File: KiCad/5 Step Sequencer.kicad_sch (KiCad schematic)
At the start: 64 parts, among them J1 RESET IN, J2 TRIG IN, J4 CV OUT, J5 TRIG OUT, Q1 2SA1015, SW1 SW_DPST_x2, SW2 SW_DPST_x2, SW3 SW_DPST_x2, SW4 SW_DPST_x2, SW5 SW_DPST_x2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

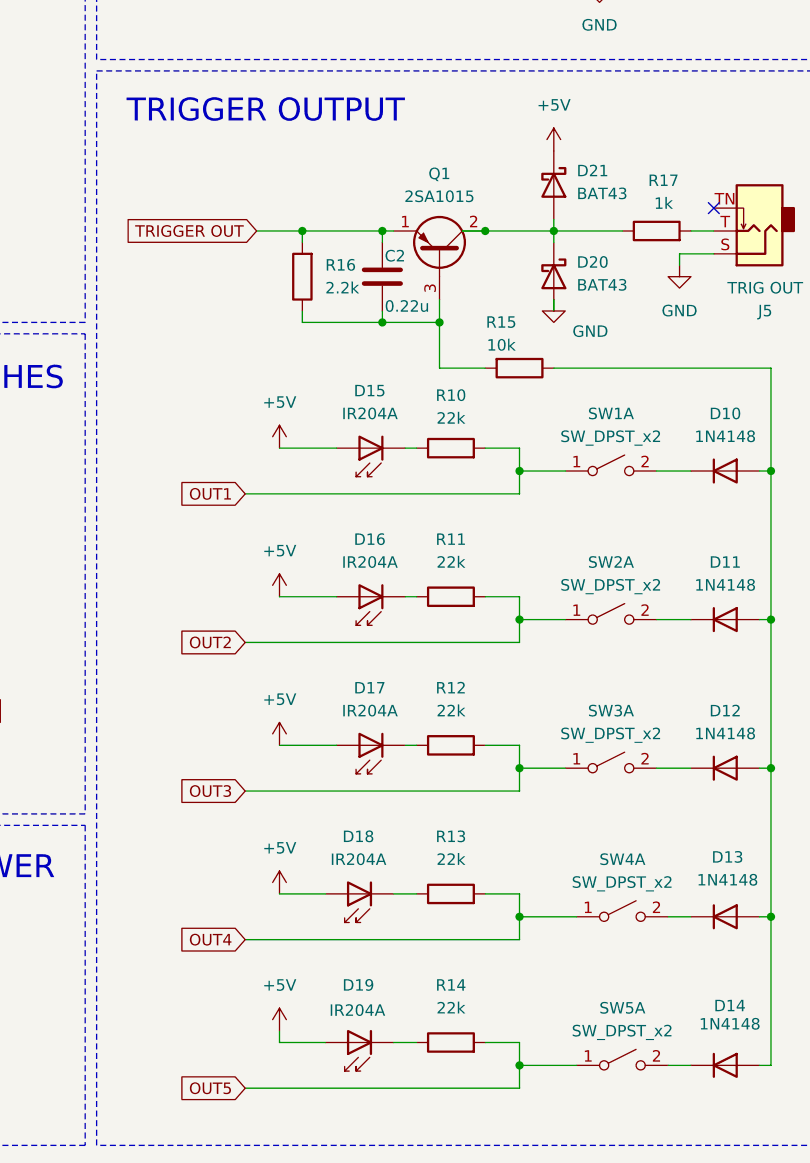
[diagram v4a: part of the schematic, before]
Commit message: adding some missing footprints
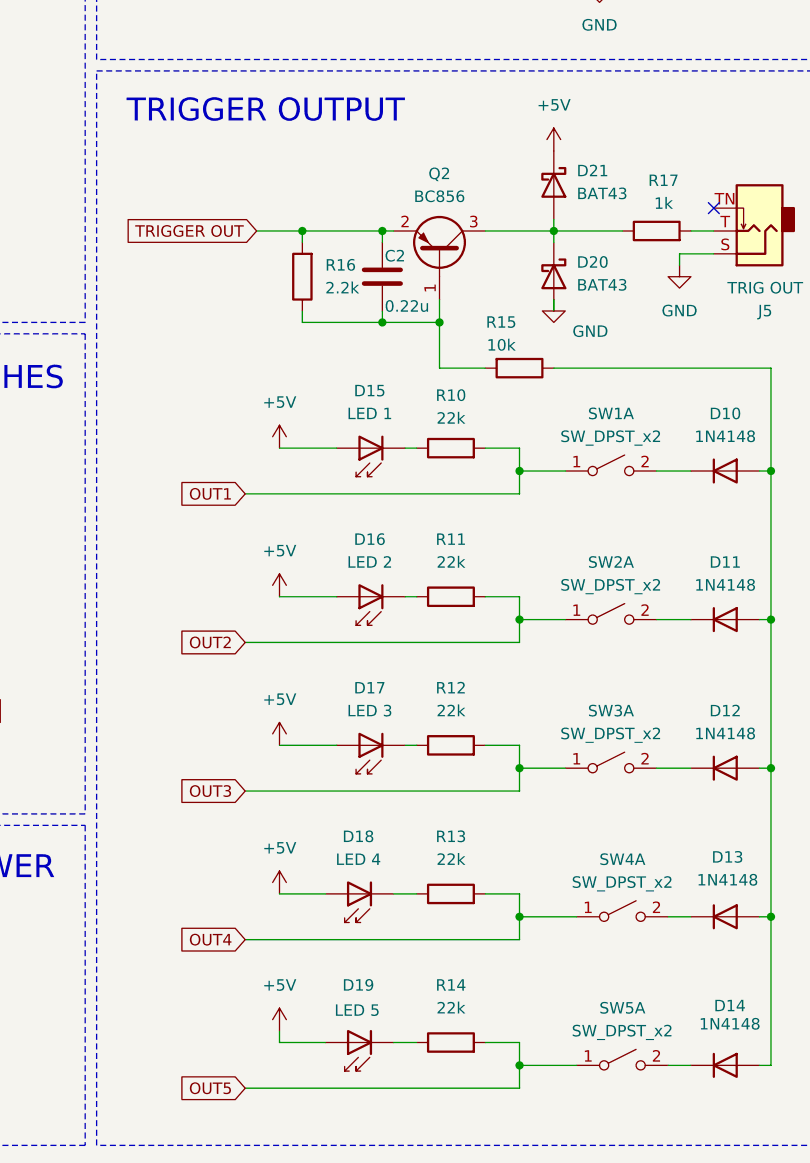
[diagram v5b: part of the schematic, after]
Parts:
- removed Q1: 2SA1015, Package_TO_SOT_THT:TO-92_Inline, symbol Transistor_BJT:2SA1015
- added Q2: BC856, Package_TO_SOT_SMD:SOT-23, symbol Transistor_BJT:BC856
- A1: footprint Module:Arduino_Nano -> Eurorack:Arduino_Nano; now left out of the parts list
- C1, C2, C3: footprint (none) -> Capacitor_SMD:C_0805_2012Metric_Pad1.18x1.45mm_HandSolder; now left out of the parts list
- C12, C13: now left out of the parts list
- D1, D10, D11, D12, D13, D14, D2, D20, D21, D3, D4, D5, D6, D7, D8, D9: footprint Diode_THT:D_DO-35_SOD27_P7.62mm_Horizontal -> Diode_SMD:D_SOD-323_HandSoldering; now left out of the parts list
- D15: value IR204A -> LED 1; footprint LED_THT:LED_D3.0mm_IRBlack -> LED_THT:LED_D3.0mm_Clear; now left out of the parts list
- D16: value IR204A -> LED 2; footprint LED_THT:LED_D3.0mm_IRBlack -> LED_THT:LED_D3.0mm_Clear; now left out of the parts list
- D17: value IR204A -> LED 3; footprint LED_THT:LED_D3.0mm_IRBlack -> LED_THT:LED_D3.0mm_Clear; now left out of the parts list
- D18: value IR204A -> LED 4; footprint LED_THT:LED_D3.0mm_IRBlack -> LED_THT:LED_D3.0mm_Clear; now left out of the parts list
- D19: value IR204A -> LED 5; footprint LED_THT:LED_D3.0mm_IRBlack -> LED_THT:LED_D3.0mm_Clear; now left out of the parts list
- J1, J2, J4, J5: footprint (none) -> Eurorack:Jack_3.5mm_QingPu_WQP-PJ398SM_Vertical; now left out of the parts list
- R1, R10, R11, R12, R13, R14, R15, R16, R17, R18, R2, R3, R4, R5, R6, R7, R8, R9: footprint (none) -> Resistor_SMD:R_0805_2012Metric_Pad1.20x1.40mm_HandSolder; now left out of the parts list
- RV1, RV2, RV3, RV4, RV5, RV6, RV7: footprint (none) -> Eurorack:Potentiometer_Alpha_RD901F_Vertical_Alt; now left out of the parts list
- SW1, SW2, SW3, SW4, SW5: footprint (none) -> Eurorack:Switch_Toggle_Dailywell_MS1T1B1M2QES_SPDT; now left out of the parts list
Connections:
- net TRIGGER OUT: now also Q2.2 (E)
- net at C2.2, R15.2, R16.1: now also Q2.1 (B)
- net at D20.1 (K), D21.2 (A), R17.1: now also Q2.3 (C)

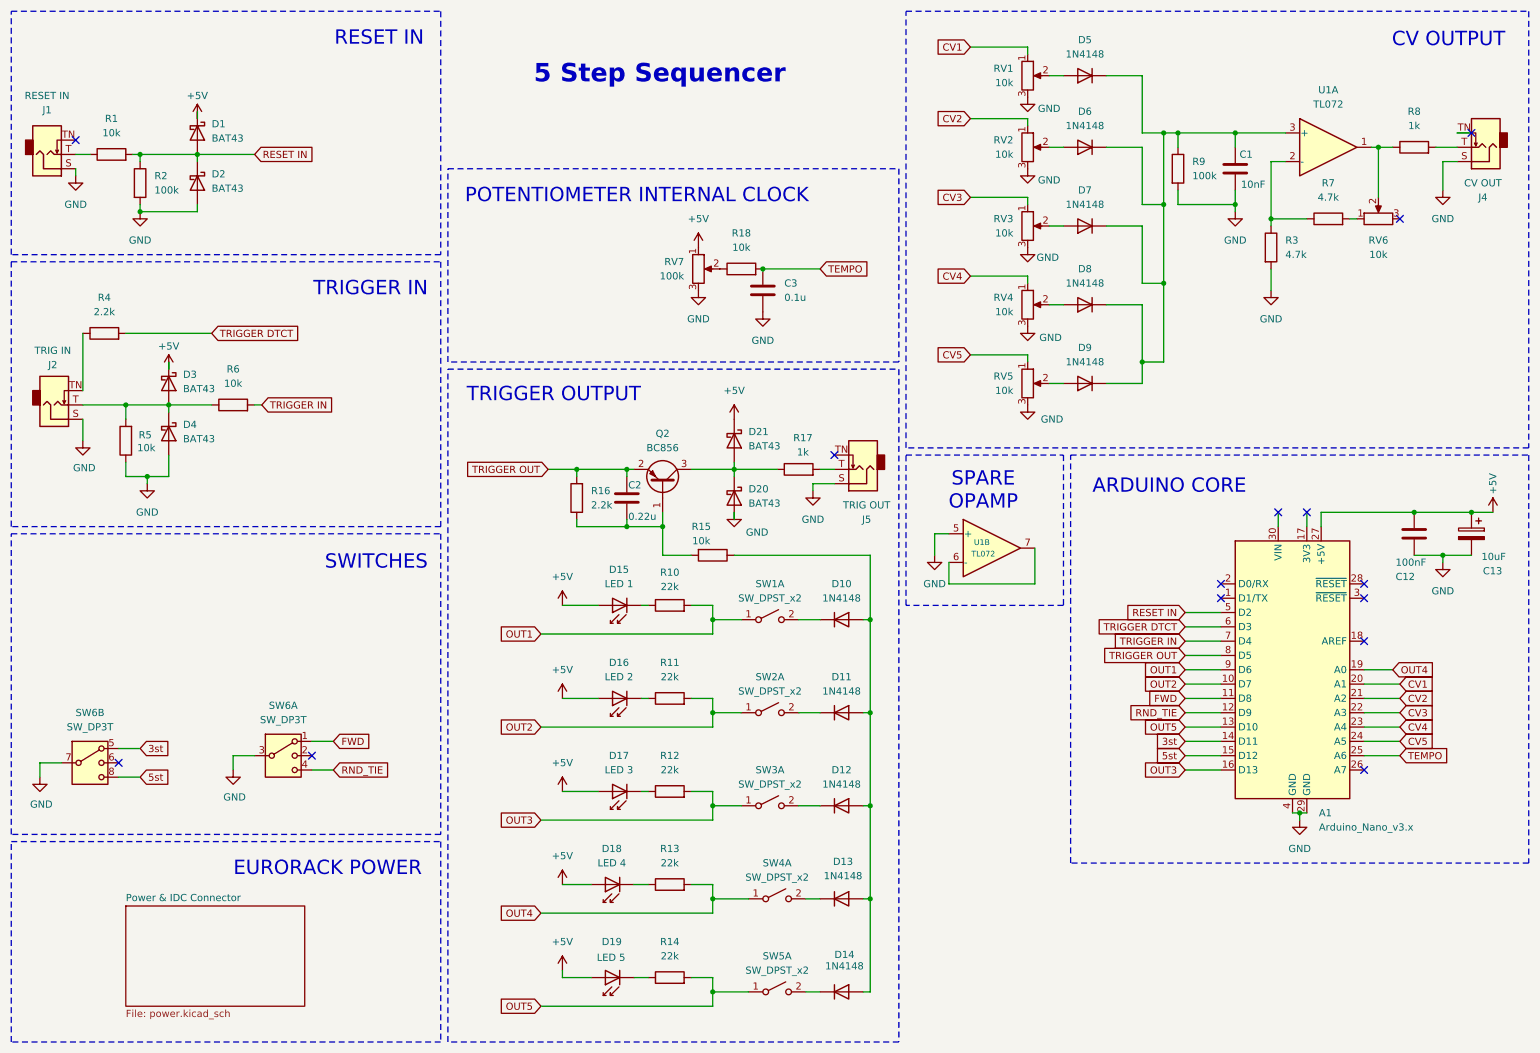
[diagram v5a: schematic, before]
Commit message: Changing Toggle Switch Foorptint
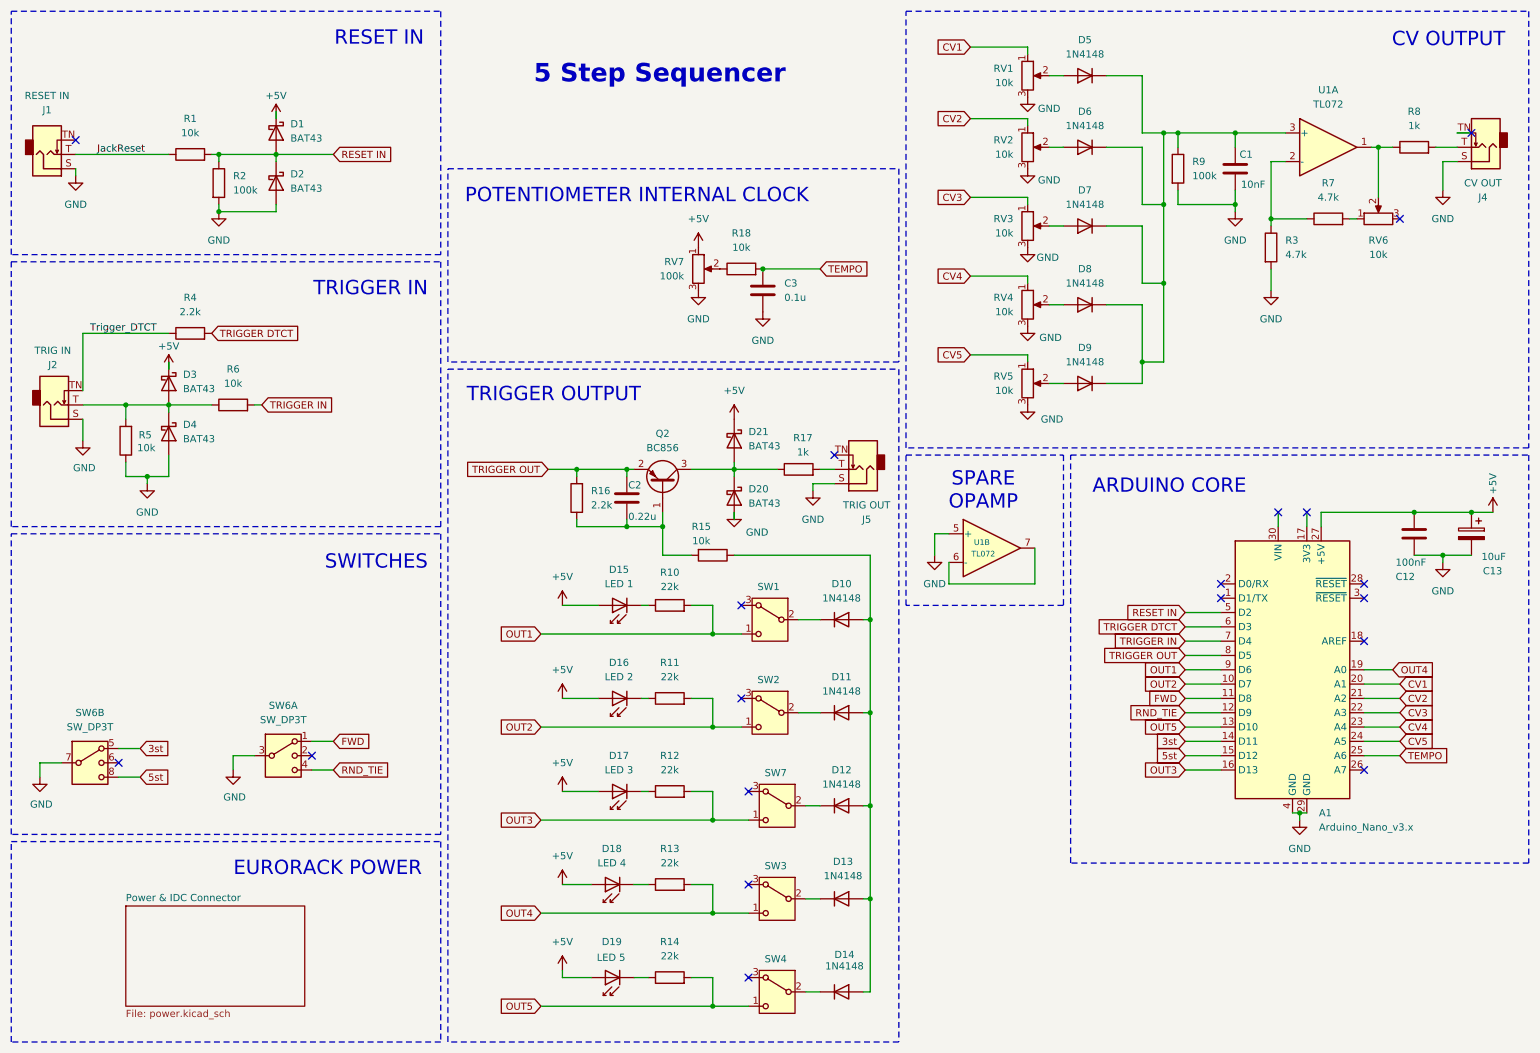
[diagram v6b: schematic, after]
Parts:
- removed SW1, SW2, SW3, SW4, SW5: SW_DPST_x2, Eurorack:Switch_Toggle_Dailywell_MS1T1B1M2QES_SPDT, symbol Switch:SW_DPST_x2
- added SW1, SW2, SW3, SW4, SW7: SW_SPDT_321, Eurorack:Switch_Toggle_Dailywell_MS1T1B1M2QES_SPDT, symbol Switch:SW_SPDT_321
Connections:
- net OUT1: now also SW1.1 (C)
- net OUT2: now also SW2.1 (C)
- net OUT3: now also SW7.1 (C)
- net OUT4: now also SW3.1 (C)
- net OUT5: now also SW4.1 (C)
- net Trigger_DTCT: now reaches J2.TN, R4.1
- net at D11.1 (K): now also SW2.2 (B)
- net at D10.1 (K): now also SW1.2 (B)
- net JackReset: now reaches J1.T, R1.1
- net at D13.1 (K): now also SW3.2 (B)
- net at D12.1 (K): now also SW7.2 (B)
- net at D14.1 (K): now also SW4.2 (B)
- no-connect marks 14 -> 19
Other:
- moved on the sheet: D1, D2, R1, R2, R4

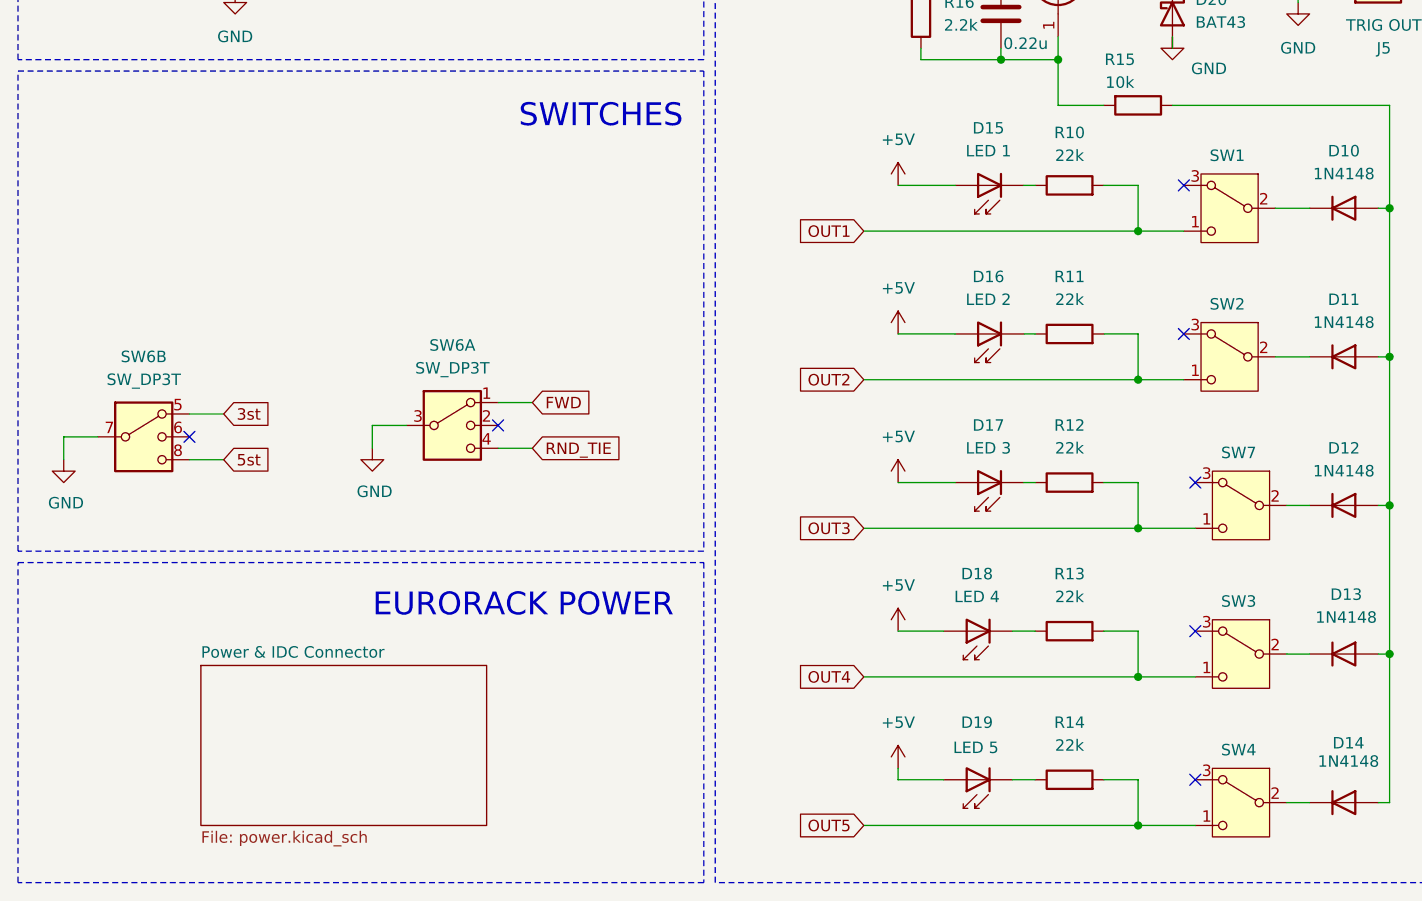
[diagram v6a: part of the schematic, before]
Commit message: adding last missing footprints
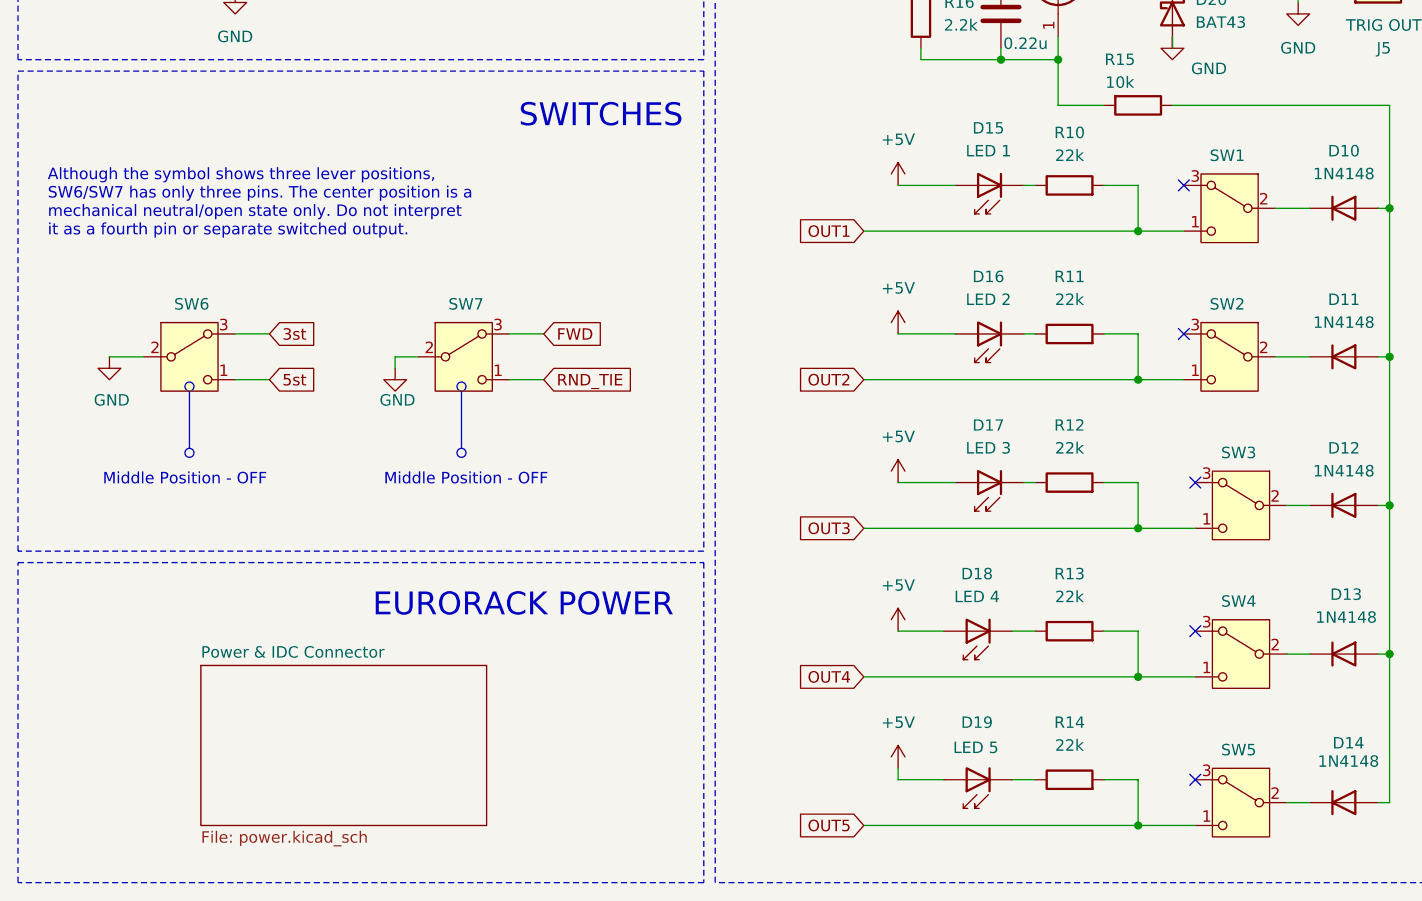
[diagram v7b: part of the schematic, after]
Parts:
- removed SW6: SW_DP3T, symbol Switch:SW_DP3T
- added SW6, SW7: SW_SPDT_321, Eurorack:Switch_Toggle_Dailywell_MS1T1B1M2QES_SPDT, symbol Switch:SW_SPDT_321
- U1: footprint (none) -> Package_SO:JEITA_SOIC-8_3.9x4.9mm_P1.27mm; now left out of the parts list
- renumbered SW7 to SW3, SW3 to SW4, SW4 to SW5
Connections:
- net 3st: now also SW6.3 (A)
- net 5st: now also SW6.1 (C)
- net FWD: now also SW7.3 (A)
- net GND: now also SW6.2 (B), SW7.2 (B)
- net RND_TIE: now also SW7.1 (C)
- no-connect marks 19 -> 17
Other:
- note added: "Although the symbol shows three lever positions, SW6/SW7 has only three pins. The center position is a mechanical neutral/open state only. Do not interpret it as a fourth pin or separate switched output."
- note added: "Middle Position - OFF"

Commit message: new footprint for tl072
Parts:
- U1: footprint Package_SO:JEITA_SOIC-8_3.9x4.9mm_P1.27mm -> Package_SO:SOIC-8_3.9x4.9mm_P1.27mm
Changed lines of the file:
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@@
 			)
 		)
-		(property "Footprint" "Package_SO:JEITA_SOIC-8_3.9x4.9mm_P1.27mm"
+		(property "Footprint" "Package_SO:SOIC-8_3.9x4.9mm_P1.27mm"
 			(at 247.65 38.1 0)
 			(effects
@@
 			)
 		)
-		(property "Footprint" "Package_SO:JEITA_SOIC-8_3.9x4.9mm_P1.27mm"
+		(property "Footprint" "Package_SO:SOIC-8_3.9x4.9mm_P1.27mm"
 			(at 187.96 109.22 0)
 			(effects
